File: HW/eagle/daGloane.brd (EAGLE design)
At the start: 105 x 90 mm, 66 parts, among them IC1 MCP1252-33X50, Q1 MOSFET-PCHANNELSMD, U1 STM32F10XTXU6

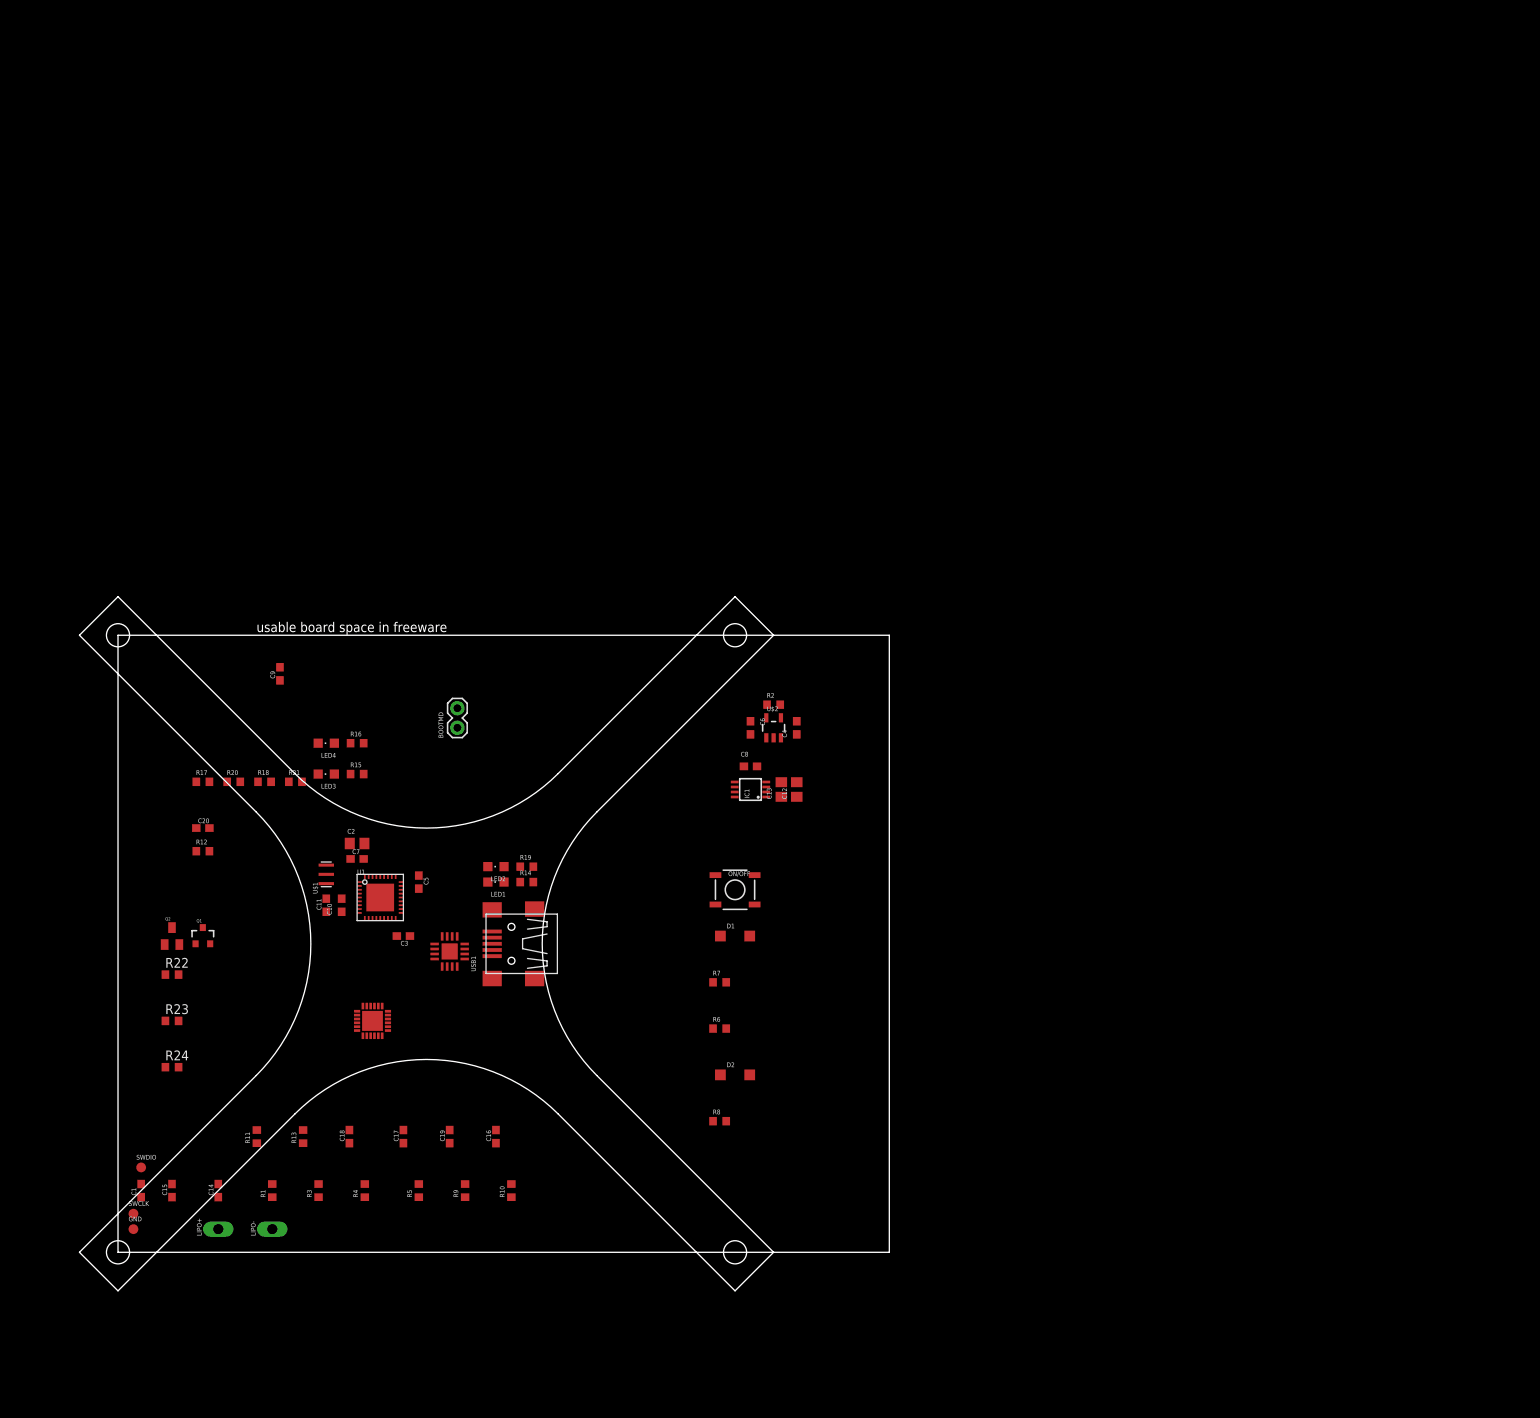
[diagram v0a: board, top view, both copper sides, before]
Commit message: Boad outlines for hextronik BLDC motor and X-Twin DC Motor
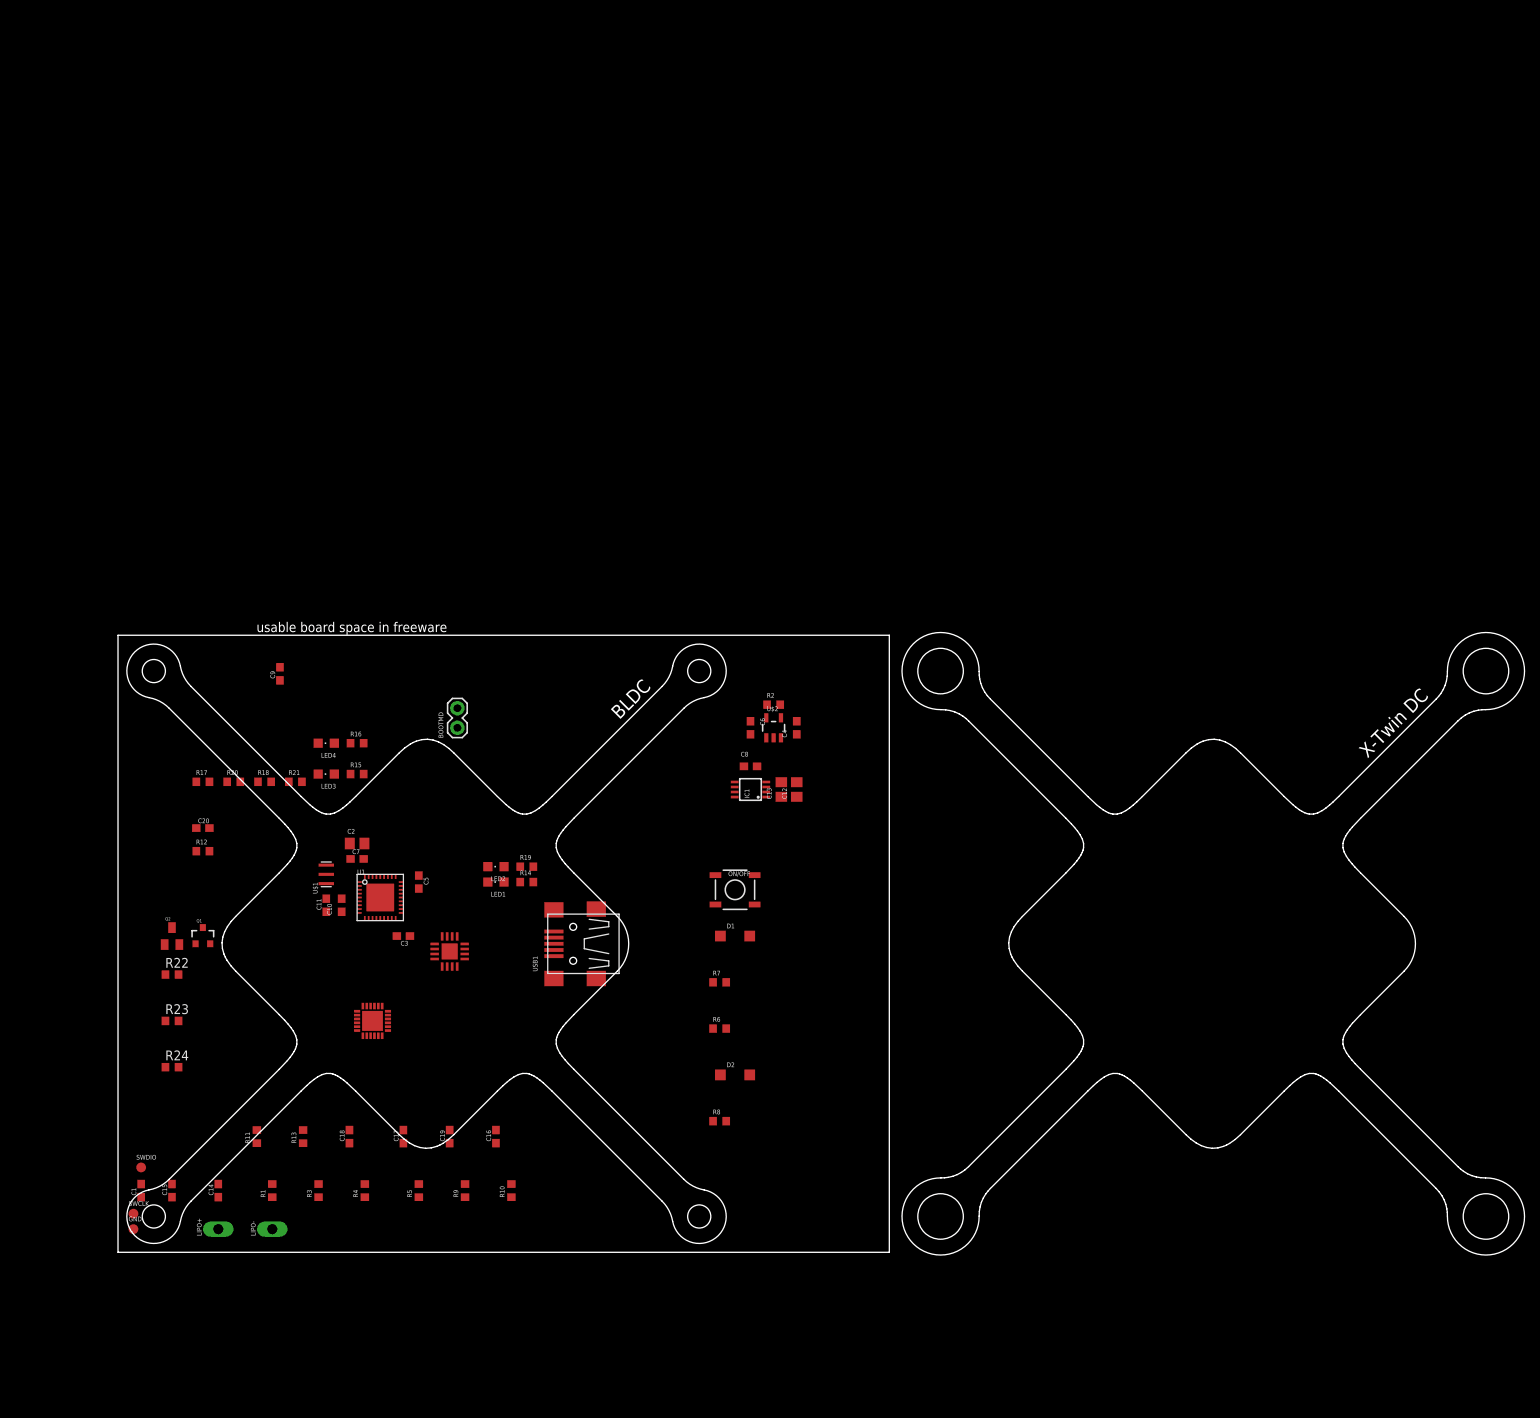
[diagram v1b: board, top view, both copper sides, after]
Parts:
- moved USB1 8.00 mm to (59.0, 40.0)
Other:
- board size 105 x 90 mm -> 182.4 x 80.7 mm
- board text added: "BLDC"
- board text added: "X-Twin DC"

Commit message: another pcb outline added
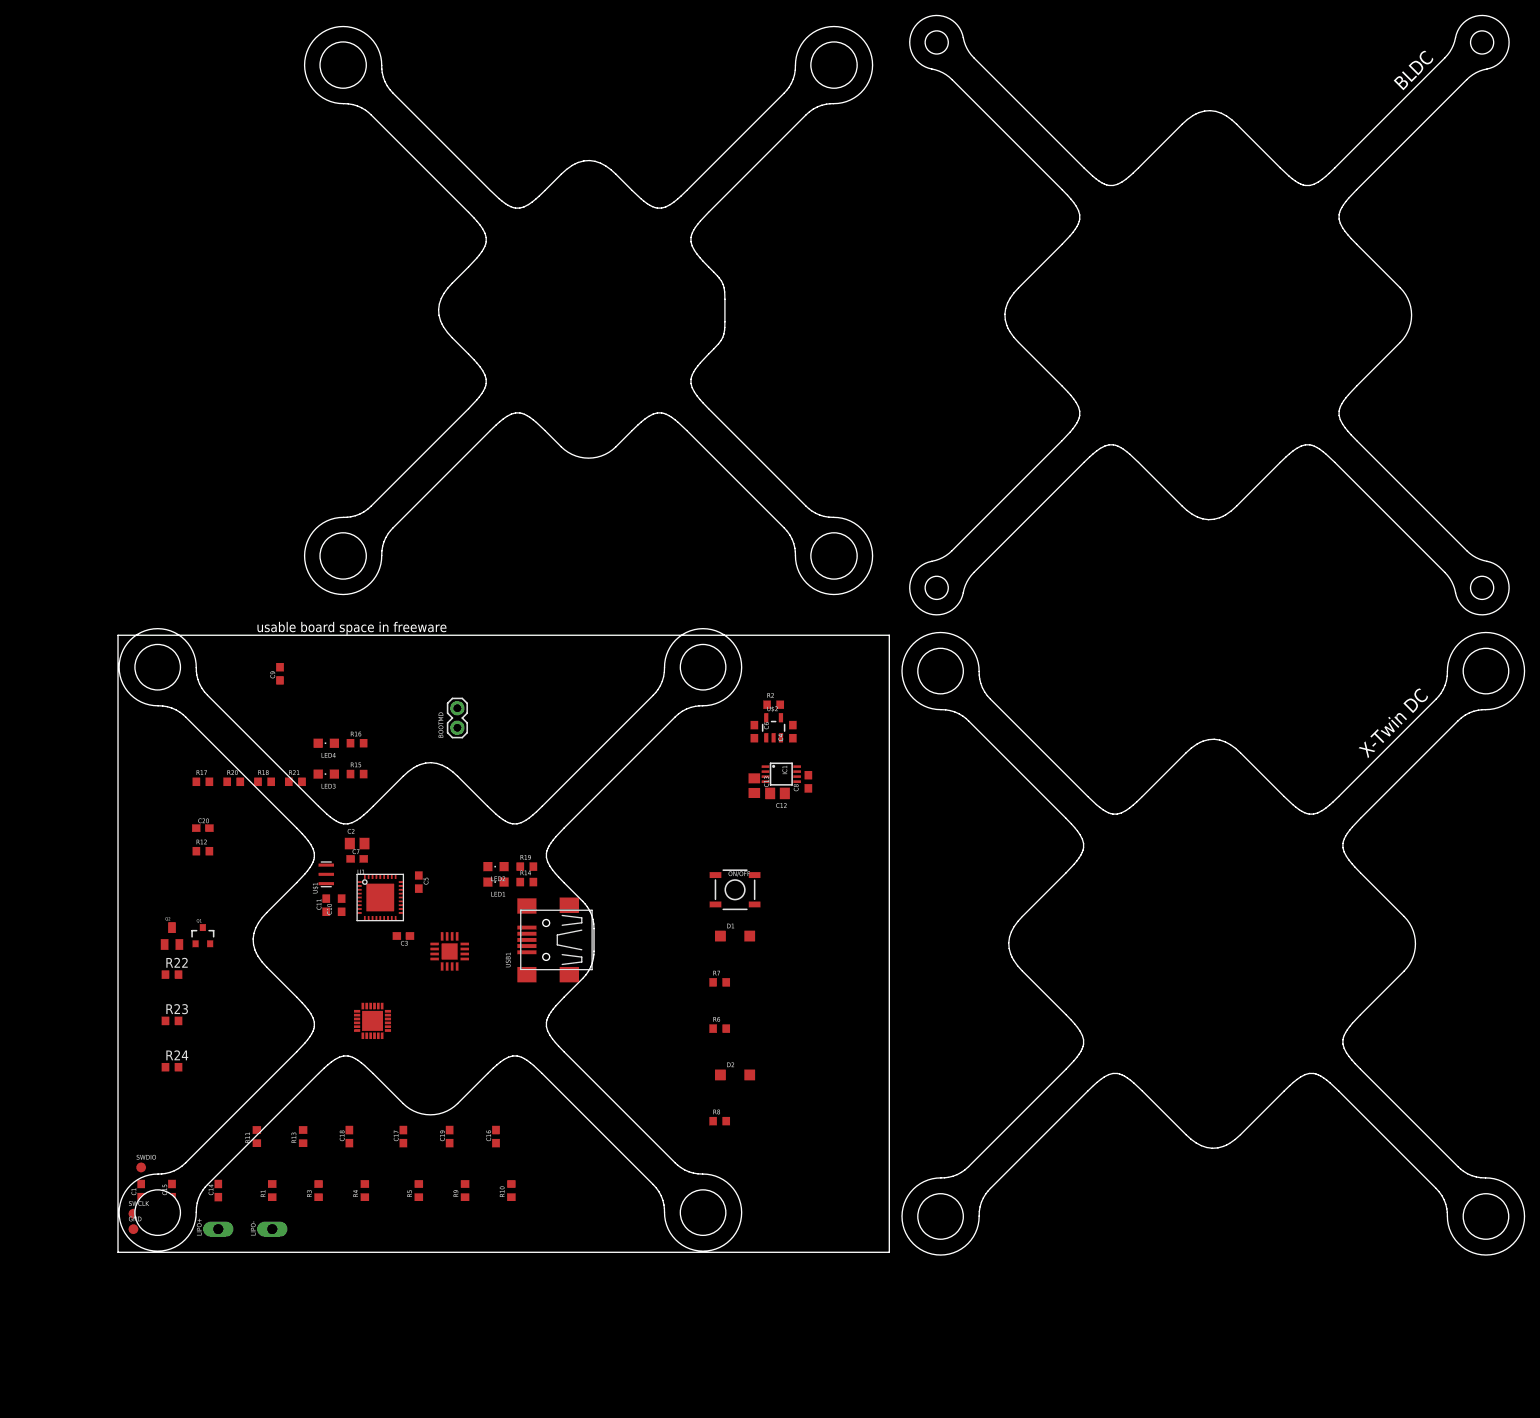
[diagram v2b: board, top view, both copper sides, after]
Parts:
- moved C8 7.76 mm to (89.5, 61.0), turned to 90 degrees
- moved IC1 4.47 mm to (86.0, 62.0), turned to 270 degrees
- moved C13 3.54 mm to (82.5, 60.5), turned to 270 degrees
- moved USB1 3.54 mm to (55.5, 40.5)
- moved C12 2.55 mm to (85.5, 59.5), turned to 180 degrees
- moved C4 0.71 mm to (87.5, 67.5)
- moved C6 0.71 mm to (82.5, 67.5)
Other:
- board size 182.4 x 80.7 mm -> 182.4 x 160.7 mm

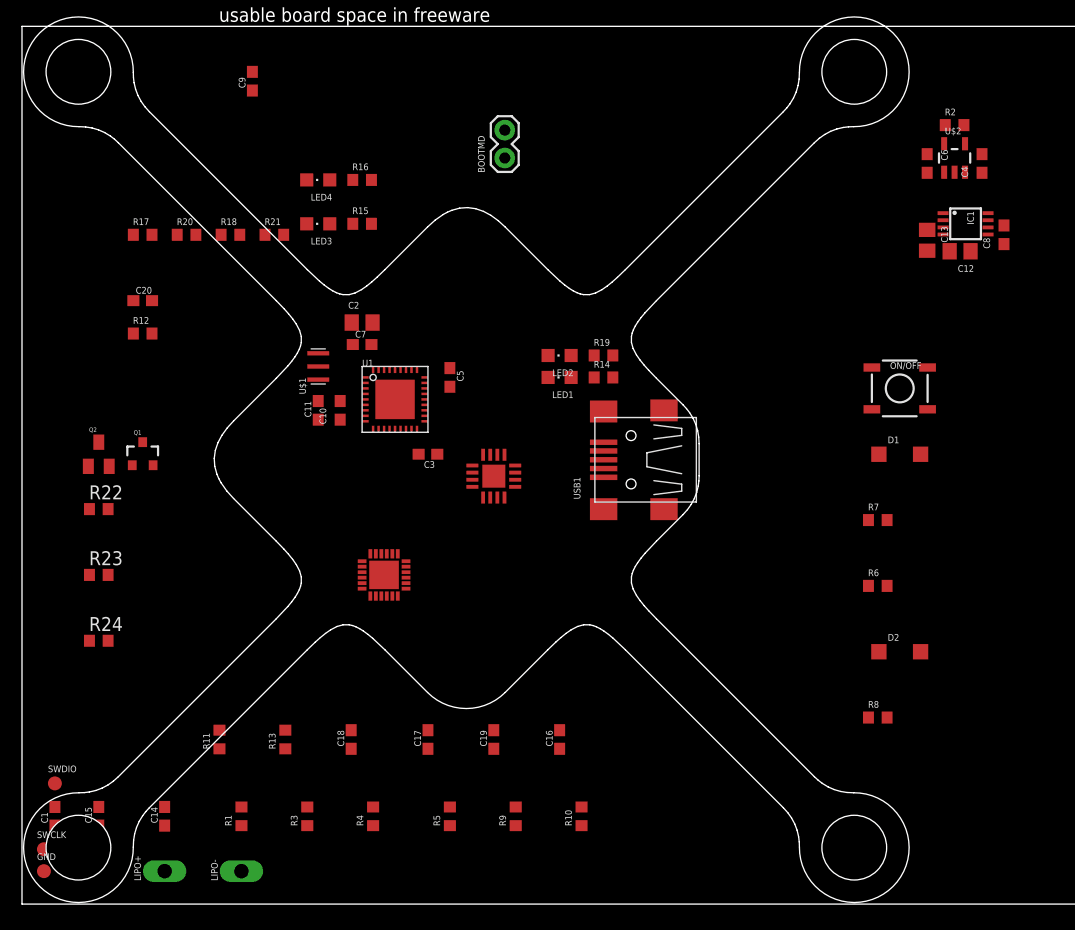
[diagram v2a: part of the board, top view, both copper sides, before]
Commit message: package outline for MPU600 package added
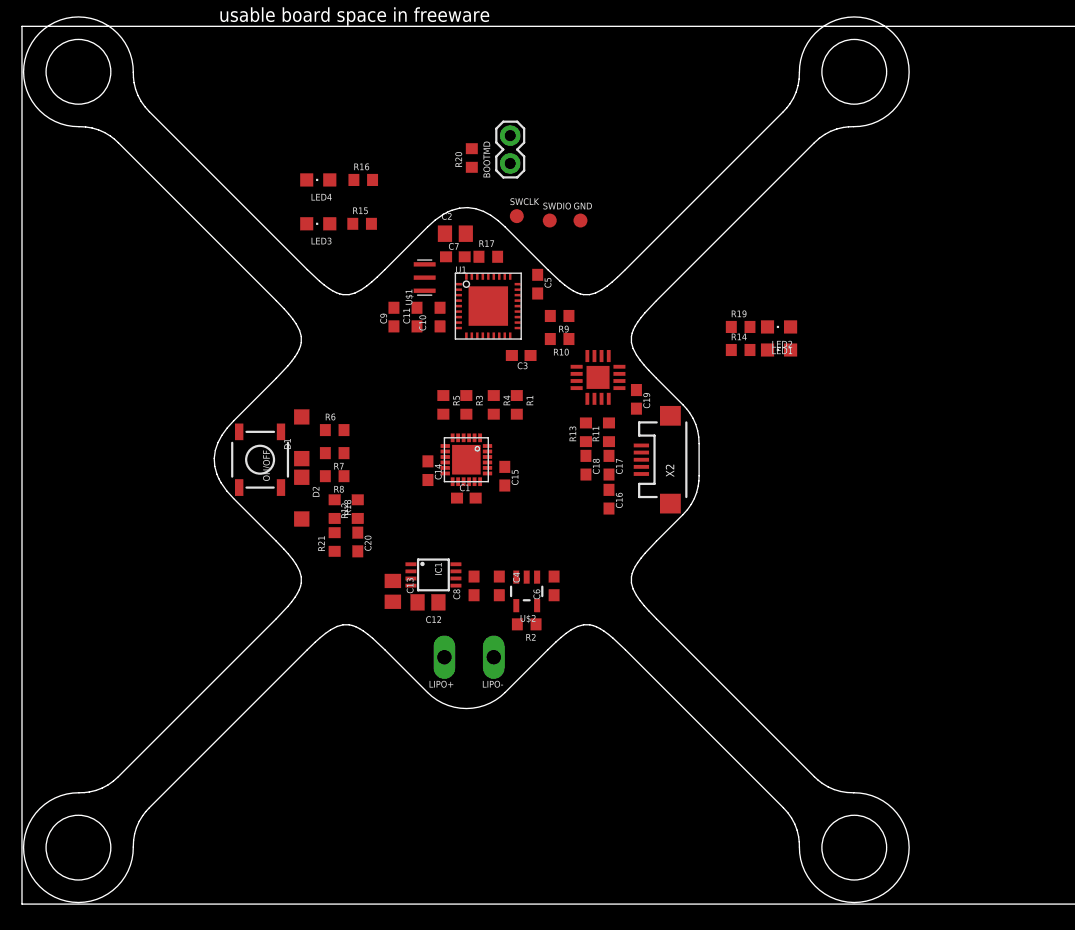
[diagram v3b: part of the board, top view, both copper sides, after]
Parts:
- removed Q1: MOSFET-PCHANNELSMD, SparkFun-DiscreteSemi:SOT23-3
- removed Q2: (no value), SparkFun-DiscreteSemi:SOT23
- removed R22, R23: 10k, rcl:R0603
- removed R24: 3.3k, rcl:R0603
- removed USB1: USB-MB-S2, con-usb:USB-MP-S2
- added X2: USB-MICROB, SparkFun-Connectors:USB-MICROB
- R1, R3, R4, R5: value 27R -> 1k
- moved GND 76.9 mm to (50.9, 62.3)
- moved SWCLK 72.0 mm to (45.1, 62.7)
- moved SWDIO 68.3 mm to (48.1, 62.3)
- moved R2 59.9 mm to (46.0, 25.5), turned to 180 degrees
- moved ON/OFF 58.7 mm to (21.7, 40.5), turned to 270 degrees
- moved C4 58.5 mm to (43.5, 29.0), turned to 270 degrees
- moved C13 58.3 mm to (33.8, 28.5)
- moved C12 58.1 mm to (37.0, 27.5)
- moved IC1 58.1 mm to (37.5, 30.0)
- moved C8 57.9 mm to (41.2, 29.0)
- moved D2 56.3 mm to (25.5, 37.0), turned to 270 degrees
- moved U$2 55.5 mm to (46.0, 28.5), turned to 180 degrees
- moved D1 54.5 mm to (25.5, 42.5), turned to 90 degrees
- moved R8 54.2 mm to (28.5, 39.0), turned to 180 degrees
- moved R6 51.5 mm to (28.5, 43.2)
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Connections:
- removed net N$15: LED2.A, R19.1
- removed net N$26: Q2.1, R24.1
- removed net N$7: Q1.1, Q2.3, R22.1
- removed net VMOT: Q1.3
- new net N$1: LED2.C, R19.2
- net D+: now also X2.D+; no longer USB1.D+
- net D-: now also X2.D-; no longer USB1.D-
- net GND: now also X2.GND; no longer Q2.2, R23.1, U$3.14, U$3.15, U$3.16, U$3.17, U$3.2, U$3.3, U$3.4, U$3.5, USB1.GND
- net LIPO: no longer Q1.2, R22.2
- net N$11: now also R14.1; no longer LED1.C
- net N$12: now also R19.1; no longer LED2.C
- net N$14: now also LED1.C, R14.2; no longer LED1.A, R14.1
- net VBUS: now also X2.VBUS; no longer USB1.VBUS
- net VCC: no longer R23.2, R24.2
- net VCCIO: now also LED1.A, LED2.A; no longer R14.2, R19.2

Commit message: pin assignment of µC changed  pwm outputs for the motors are now on PB0,PB1,PB4 and PB5. Those I/Os can be used with TIM3
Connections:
- removed net MOT1: U1.8
- removed net MOT2: U1.20
- removed net MOT3: U1.29
- net PWR_OFF: no longer U1.16
- net PWR_ON_µC: no longer U1.15
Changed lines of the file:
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@@
 <signal name="PWR_OFF">
 <contactref element="R6" pad="2"/>
-<contactref element="U1" pad="16"/>
-<wire x1="29.35" y1="43.2" x2="43.5" y2="51.8" width="0" layer="19" extent="1-1"/>
 </signal>
 <signal name="N$23">
@@
 <signal name="PWR_ON_µC">
 <contactref element="D2" pad="A"/>
-<contactref element="U1" pad="15"/>
-<wire x1="25.5" y1="35.1" x2="43" y2="51.8" width="0" layer="19" extent="1-1"/>
 </signal>
 <signal name="N$2">
@@
 <contactref element="U1" pad="9"/>
 </signal>
-<signal name="MOT2">
-<contactref element="U1" pad="20"/>
-</signal>
-<signal name="MOT3">
-<contactref element="U1" pad="29"/>
-</signal>
-<signal name="MOT1">
-<contactref element="U1" pad="8"/>
-</signal>
 <signal name="MOT4">
